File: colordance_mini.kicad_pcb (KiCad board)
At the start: 2 copper layers, 132.5 x 105 mm, 42 parts, among them J1 CONN_02X08, SW1 Rotary_Encoder, SW2 Rotary_Encoder, SW3 Rotary_Encoder, SW4 Rotary_Encoder

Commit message: Add front panel SVG v1.0
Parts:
- RV1, RV2, RV3, RV4, RV5, RV6: footprint homebrew:BOURNS_SLIDE_POT -> homebrew:BOURNS_SLIDE_POT_45MM
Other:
- board text added: "10mm"

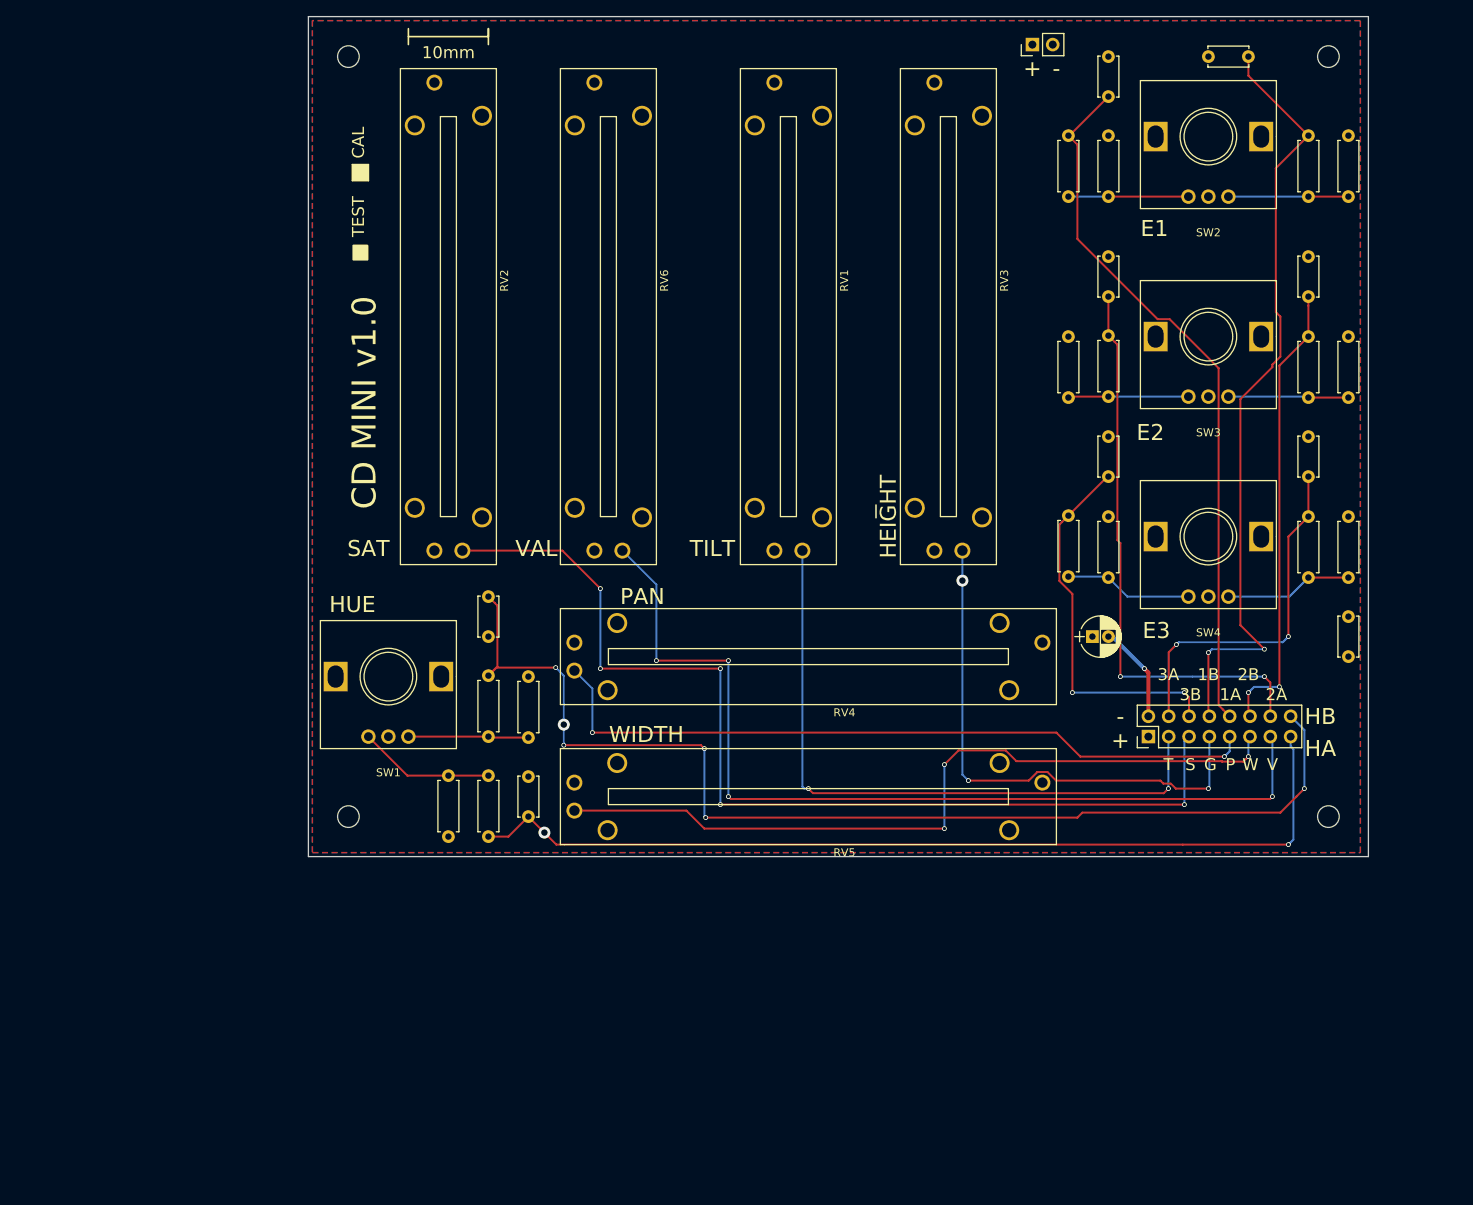
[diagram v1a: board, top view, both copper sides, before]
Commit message: Associate footprints
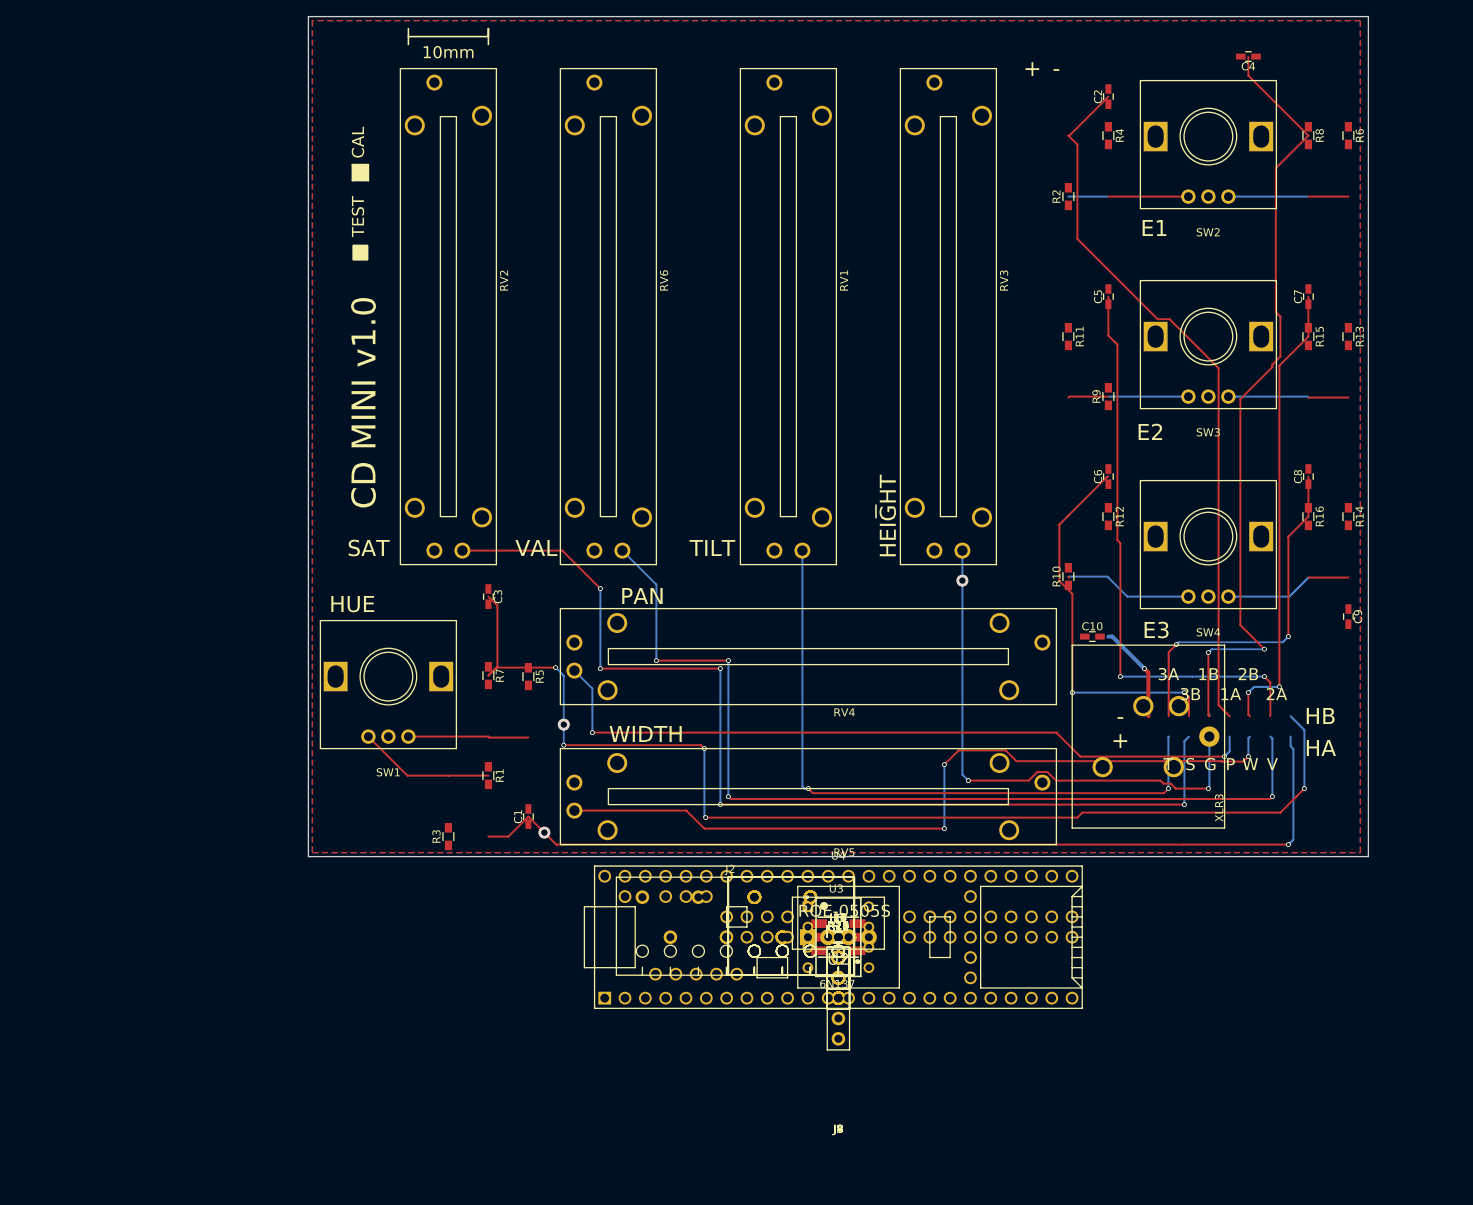
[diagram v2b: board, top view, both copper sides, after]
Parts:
- removed REF** (x4): MountingHole_2.7mm_M2.5, Mounting_Holes:MountingHole_2.7mm_M2.5
- removed REF**: Pin_Header_Straight_1x02_Pitch2.54mm, Pin_Headers:Pin_Header_Straight_1x02_Pitch2.54mm
- added C11: .01uF, Capacitors_SMD:C_0603_HandSoldering, F.Cu at (123.8, 132.6)
- added C12: 10uF, Capacitors_SMD:C_0603_HandSoldering, F.Cu at (123.8, 132.6)
- added D1: APA102C, Sparkfun-LED:APA102C, F.Cu at (123.8, 132.6)
- added J10: CONN_01X06, Pin_Headers:Pin_Header_Straight_1x06_Pitch2.54mm, F.Cu at (123.8, 132.6)
- added J11, J12, J17, J5: CONN_01X04, Pin_Headers:Pin_Header_Straight_1x04_Pitch2.54mm, F.Cu at (123.8, 132.6)
- added J13, J14, J15, J16, J6: CONN_01X03, Pin_Headers:Pin_Header_Straight_1x03_Pitch2.54mm, F.Cu at (123.8, 132.6)
- added J2: CONN_01X08, homebrew:1985250_phoenix_8pos_3.5mm, F.Cu at (123.8, 132.6)
- added J3, J7, J8, J9: CONN_01X04, homebrew:1985218_phoenix_4pos_3.5mm, F.Cu at (123.8, 132.6)
- added J4: CONN_01X03, homebrew:1985218_phoenix_4pos_3.5mm, F.Cu at (123.8, 132.6)
- added R17, R18, R19, R20, R21: 10k, Resistors_SMD:R_0603_HandSoldering, F.Cu at (123.8, 132.6)
- added R22: 470, Resistors_SMD:R_0603_HandSoldering, F.Cu at (123.8, 132.6)
- added R23, R24, R25: 4k7, Resistors_SMD:R_0603_HandSoldering, F.Cu at (123.8, 132.6)
- added U2: ROE-0505S, arduino-micro-dmx:ROE-0505S, F.Cu at (123.8, 132.6)
- added U3: 6N137, 6N137:DIP762W50P254L977H451Q8, F.Cu at (123.8, 132.6)
- added U4: Teensy3.5, teensy:Teensy35_36, F.Cu at (123.8, 132.6)
- C1, C2, C3, C4, C5, C6, C7, C9: footprint Capacitors_THT:C_Disc_D5.0mm_W2.5mm_P5.00mm -> Capacitors_SMD:C_0603_HandSoldering
- C10: value 10uF -> .01uF; footprint Capacitors_THT:CP_Radial_D5.0mm_P2.00mm -> Capacitors_SMD:C_0603_HandSoldering
- C8: value .01uF -> 10uF; footprint Capacitors_THT:C_Disc_D5.0mm_W2.5mm_P5.00mm -> Capacitors_SMD:C_0603_HandSoldering
- J1: value CONN_02X08 -> XLR3; footprint Pin_Headers:Pin_Header_Straight_2x08_Pitch2.54mm -> shardy:XLR-NC3FA
- R1: value 10k -> 120; footprint Resistors_THT:R_Axial_DIN0207_L6.3mm_D2.5mm_P7.62mm_Horizontal -> Resistors_SMD:R_0603_HandSoldering
- R10, R11, R12, R13, R14, R15, R16, R6, R7, R8, R9: footprint Resistors_THT:R_Axial_DIN0207_L6.3mm_D2.5mm_P7.62mm_Horizontal -> Resistors_SMD:R_0603_HandSoldering
- R2: value 10k -> 3k3; footprint Resistors_THT:R_Axial_DIN0207_L6.3mm_D2.5mm_P7.62mm_Horizontal -> Resistors_SMD:R_0603_HandSoldering
- R3: value 10k -> 1k; footprint Resistors_THT:R_Axial_DIN0207_L6.3mm_D2.5mm_P7.62mm_Horizontal -> Resistors_SMD:R_0603_HandSoldering
- R4, R5: value 10k -> 562; footprint Resistors_THT:R_Axial_DIN0207_L6.3mm_D2.5mm_P7.62mm_Horizontal -> Resistors_SMD:R_0603_HandSoldering
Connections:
- C1 pad 1: HUE_A -> HUE_0_A
- C10 pad 1: VCC -> TEMPO_B
- C2 pad 1: E1_A -> HUE_1_A
- C3 pad 1: HUE_B -> HUE_0_B
- C4 pad 1: E1_B -> HUE_1_B
- C5 pad 1: E2_A -> HUE_2_A
- C6 pad 1: E3_A -> TEMPO_A
- C7 pad 1: E2_B -> VDMX
- C8 pad 1: E3_B -> VDMX
- C9 pad 1: VCC -> HUE_2_B
- J1 pad 1: VCC -> GND
- J1 pad 2: GND -> Net-(J1-Pad2)
- J1 pad 3: TILT -> Net-(J1-Pad3)
- R1 pad 1: Net-(R1-Pad1) -> Net-(J1-Pad2)
- R1 pad 2: HUE_A -> Net-(J1-Pad3)
- R10 pad 1: Net-(R10-Pad1) -> +3V3
- R10 pad 2: E3_A -> Net-(R10-Pad2)
- R11 pad 1: VCC -> +3V3
- R12 pad 1: VCC -> HUE_0_B
- R12 pad 2: Net-(R10-Pad1) -> Net-(R10-Pad2)
- R13 pad 1: VCC -> HUE_1_B
- R13 pad 2: Net-(R13-Pad2) -> Net-(R11-Pad2)
- R14 pad 1: VCC -> Net-(R14-Pad1)
- R14 pad 2: Net-(R14-Pad2) -> HUE_2_A
- R15 pad 1: E2_B -> Net-(R15-Pad1)
- R15 pad 2: Net-(R13-Pad2) -> TEMPO_A
- R16 pad 1: E3_B -> +3V3
- R16 pad 2: Net-(R14-Pad2) -> Net-(R14-Pad1)
- R2 pad 1: Net-(R2-Pad1) -> +BATT
- R2 pad 2: E1_A -> VBATT_DIV
- R3 pad 1: VCC -> VBATT_DIV
- R3 pad 2: Net-(R1-Pad1) -> GND
- R4 pad 1: VCC -> +5V
- R4 pad 2: Net-(R2-Pad1) -> Net-(J1-Pad2)
- R5 pad 1: VCC -> Net-(J1-Pad3)
- R5 pad 2: Net-(R5-Pad2) -> GND
- R6 pad 1: VCC -> Net-(R6-Pad1)
- R6 pad 2: Net-(R6-Pad2) -> HUE_0_A
- R7 pad 1: HUE_B -> Net-(R7-Pad1)
- R7 pad 2: Net-(R5-Pad2) -> HUE_1_A
- R8 pad 1: E1_B -> +3V3
- R8 pad 2: Net-(R6-Pad2) -> Net-(R6-Pad1)
- R9 pad 1: Net-(R11-Pad2) -> +3V3
- R9 pad 2: E2_A -> Net-(R7-Pad1)
- RV1 pad 1: VCC -> +3V3
- RV2 pad 1: VCC -> +3V3
- RV2 pad 2: SAT -> HEIGHT
- RV3 pad 1: VCC -> +3V3
- RV3 pad 2: HEIGHT -> PAN
- RV4 pad 1: VCC -> +3V3
- RV4 pad 2: PAN -> WIDTH
- RV5 pad 1: VCC -> +3V3
- RV5 pad 2: WIDTH -> DENSITY
- RV6 pad 1: VCC -> +3V3
- RV6 pad 2: VAL -> PARAM
- SW1 pad 1: Net-(R1-Pad1) -> Net-(R6-Pad1)
- SW1 pad 3: Net-(R5-Pad2) -> Net-(R10-Pad2)
- SW2 pad 1: Net-(R2-Pad1) -> Net-(R7-Pad1)
- SW2 pad 3: Net-(R6-Pad2) -> Net-(R11-Pad2)
- SW3 pad 1: Net-(R11-Pad2) -> Net-(R14-Pad1)
- SW3 pad 3: Net-(R13-Pad2) -> Net-(R18-Pad2)
- SW4 pad 1: Net-(R10-Pad1) -> Net-(R15-Pad1)
- SW4 pad 3: Net-(R14-Pad2) -> Net-(R19-Pad2)
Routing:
- net (no net): track 0.00 -> 646.6 mm, vias 0 -> 17
- net HUE_B: track 142.3 -> 0.00 mm, vias 6 -> 0
- net SAT: track 128.0 -> 0.00 mm, vias 5 -> 0
- net VAL: track 117.4 -> 0.00 mm, vias 4 -> 0
- net PARAM: track 0.00 -> 117.4 mm, vias 0 -> 4
- net HUE_A: track 116.4 -> 0.00 mm, vias 2 -> 0
- net E1_B: track 97.9 -> 0.00 mm, vias 2 -> 0
- net DENSITY: track 0.00 -> 97.3 mm, vias 0 -> 3
- net E1_A: track 88.8 -> 0.00 mm
- net E2_A: track 71.4 -> 0.00 mm, vias 2 -> 0
- net HEIGHT: track 67.1 -> 128.0 mm, vias 3 -> 5
- net VDMX: track 0.00 -> 57.5 mm, vias 0 -> 2
- net E2_B: track 57.5 -> 0.00 mm, vias 2 -> 0
- net E3_A: track 47.5 -> 0.00 mm, vias 2 -> 0
- net E3_B: track 44.8 -> 0.00 mm, vias 2 -> 0
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
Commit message: Rough placement
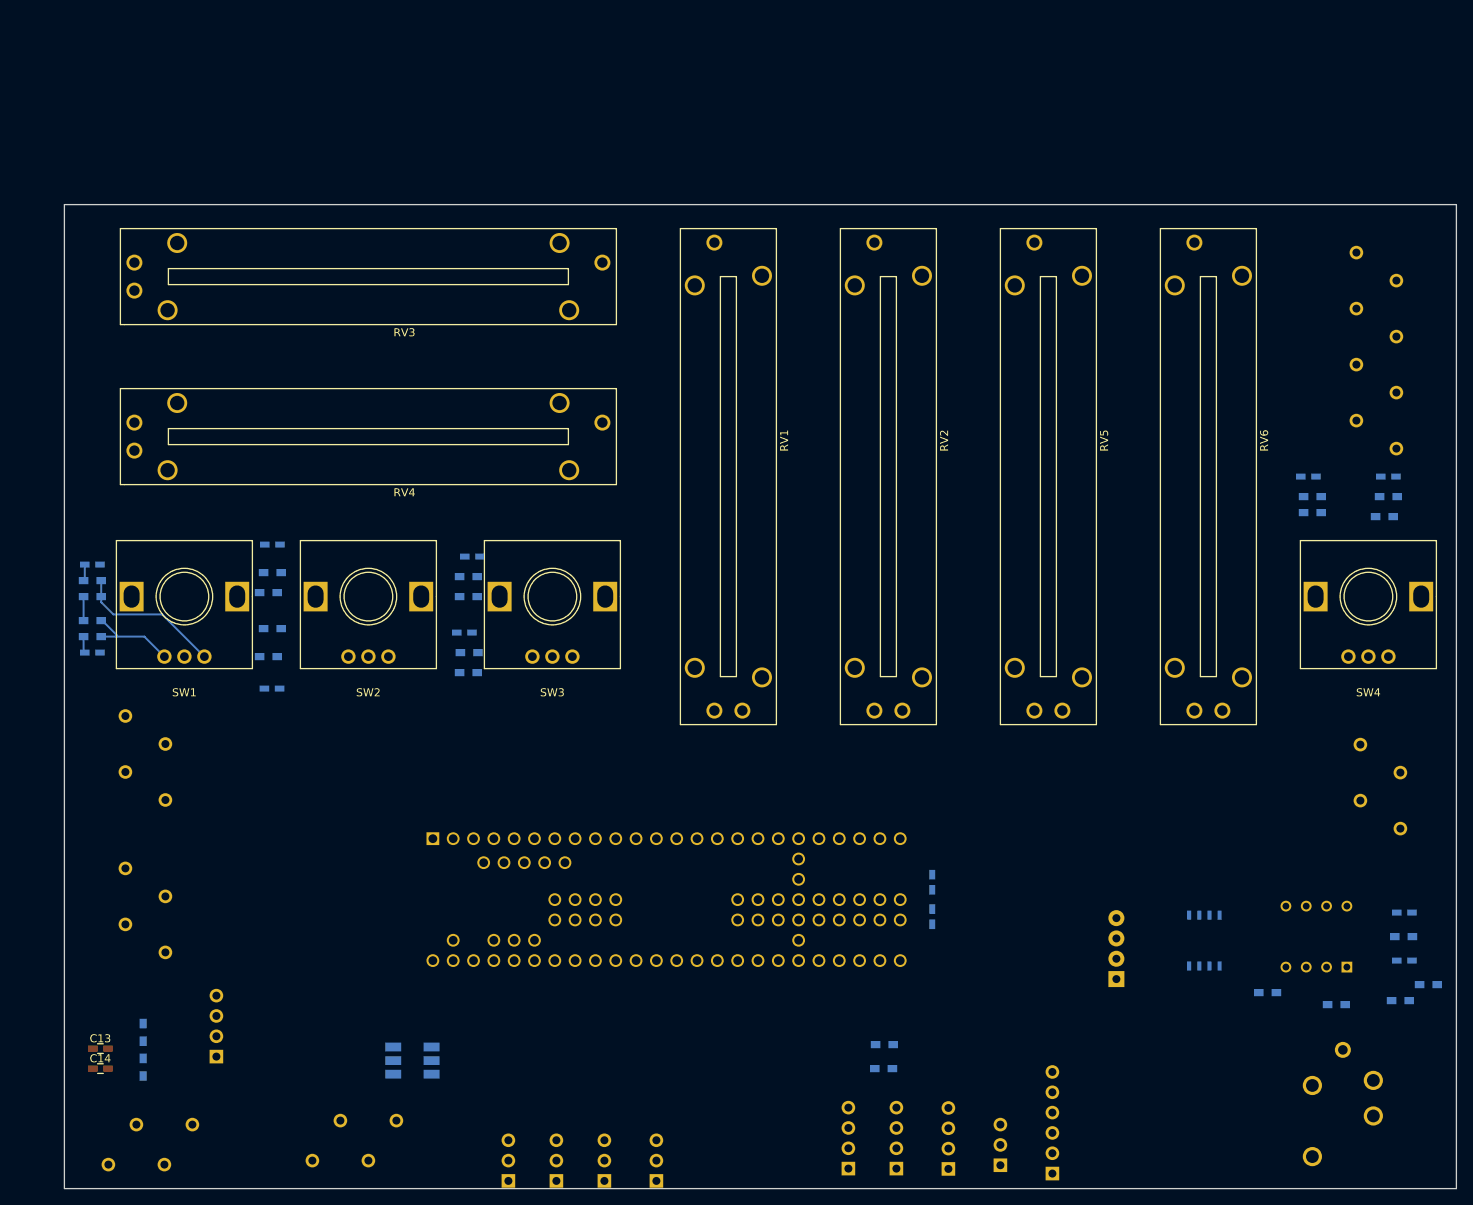
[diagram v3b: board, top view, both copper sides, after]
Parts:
- added C13: .01uF, Capacitors_SMD:C_0603_HandSoldering, F.Cu at (31.5, 146.5)
- added C14: 10uF, Capacitors_SMD:C_0603_HandSoldering, F.Cu at (31.5, 149.0)
- added U1: MAX485CSA+, SMD_Packages:SOIC-8-N, B.Cu at (169.5, 133.0)
- C1, C10, C11, C12, C2, C3, C4, C5, C6, C7, C8, C9, D1, J10, J11, J12, J13, J14, J15, J16, J17, J2, J3, J4, J5, J6, J7, J8, J9, R1, R10, R11, R12, R13, R14, R15, R16, R17, R18, R19, R2, R20, R21, R22, R23, R24, R25, R3, R4, R5, R6, R7, R8, R9, U2, U3, U4: moved to B.Cu
- J1: footprint shardy:XLR-NC3FA -> homebrew:NC3FAH; moved to B.Cu
- moved R6 169.0 mm to (30.5, 95.0), turned to 180 degrees
- moved R8 163.6 mm to (30.5, 93.0), turned to 0 degrees
- moved R2 155.8 mm to (36.8, 144.5)
- moved R13 138.7 mm to (52.5, 89.5), turned to 0 degrees
- moved C4 136.4 mm to (53.0, 83.5), turned to 0 degrees
- moved C2 128.1 mm to (53.0, 101.5), turned to 0 degrees
- moved R12 127.3 mm to (30.5, 88.0), turned to 0 degrees
- moved R10 122.0 mm to (30.5, 90.0), turned to 0 degrees
- moved SW2 119.7 mm to (65.0, 90.0)
- moved R4 114.1 mm to (194.0, 140.5), turned to 0 degrees
- moved R14 111.2 mm to (77.6, 97.0), turned to 0 degrees
- moved R9 109.9 mm to (52.5, 97.5), turned to 0 degrees
- moved R1 109.8 mm to (186.0, 141.0), turned to 0 degrees
- moved C9 109.8 mm to (78.0, 85.0), turned to 0 degrees
- moved R16 106.8 mm to (77.5, 99.5), turned to 0 degrees
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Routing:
- net (no net): track 646.6 -> 0.00 mm, vias 17 -> 0
- net HEIGHT: track 128.0 -> 0.00 mm, vias 5 -> 0
- net PARAM: track 117.4 -> 0.00 mm, vias 4 -> 0
- net DENSITY: track 97.3 -> 0.00 mm, vias 3 -> 0
- net WIDTH: track 91.7 -> 0.00 mm, vias 2 -> 0
- net TILT: track 82.3 -> 0.00 mm, vias 2 -> 0
- net VDMX: track 57.5 -> 0.00 mm, vias 2 -> 0
- net PAN: track 55.4 -> 0.00 mm, vias 2 -> 0
- net Net-(R15-Pad1): track 16.0 -> 0.00 mm
- net Net-(J1-Pad3): track 11.7 -> 0.00 mm, vias 1 -> 0
- net Net-(R19-Pad2): track 11.0 -> 0.00 mm
- net Net-(R18-Pad2): track 10.0 -> 0.00 mm
- net Net-(R7-Pad1): track 10.0 -> 0.00 mm
- net Net-(R14-Pad1): track 10.0 -> 0.00 mm
- net Net-(R11-Pad2): track 10.0 -> 0.00 mm
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- removed copper zone on B.Cu, net GND
- removed copper zone on F.Cu, net VCC
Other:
- board size 132.5 x 105 mm -> 174 x 123 mm
- rule pad_to_mask_clearance: 0.2 -> 0
- rule via_min_size: 0.45 -> 0.4
- board text added: "Logger"
- board text removed: "+"
- board text removed: "-"
- board text removed: "10mm"
- board text removed: "1A"
- board text removed: "1B"
- board text removed: "2A"
- board text removed: "2B"
- board text removed: "3A"
- board text removed: "3B"
- board text removed: "CAL"
- board text removed: "CD MINI v1.0"
- board text removed: "E1"
- board text removed: "E2"
- board text removed: "E3"
- board text removed: "G"
- board text removed: "HA"
- board text removed: "HB"
- board text removed: "HEIGHT"
- board text removed: "HUE"
- board text removed: "P"
- board text removed: "PAN"
- board text removed: "S"
- board text removed: "SAT"
- board text removed: "T"
- board text removed: "TEST"
- board text removed: "TILT"
- board text removed: "V"
- board text removed: "VAL"
- board text removed: "W"
- board text removed: "WIDTH"
